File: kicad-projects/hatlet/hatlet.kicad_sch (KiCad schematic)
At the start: 14 parts, among them U1 RP2040

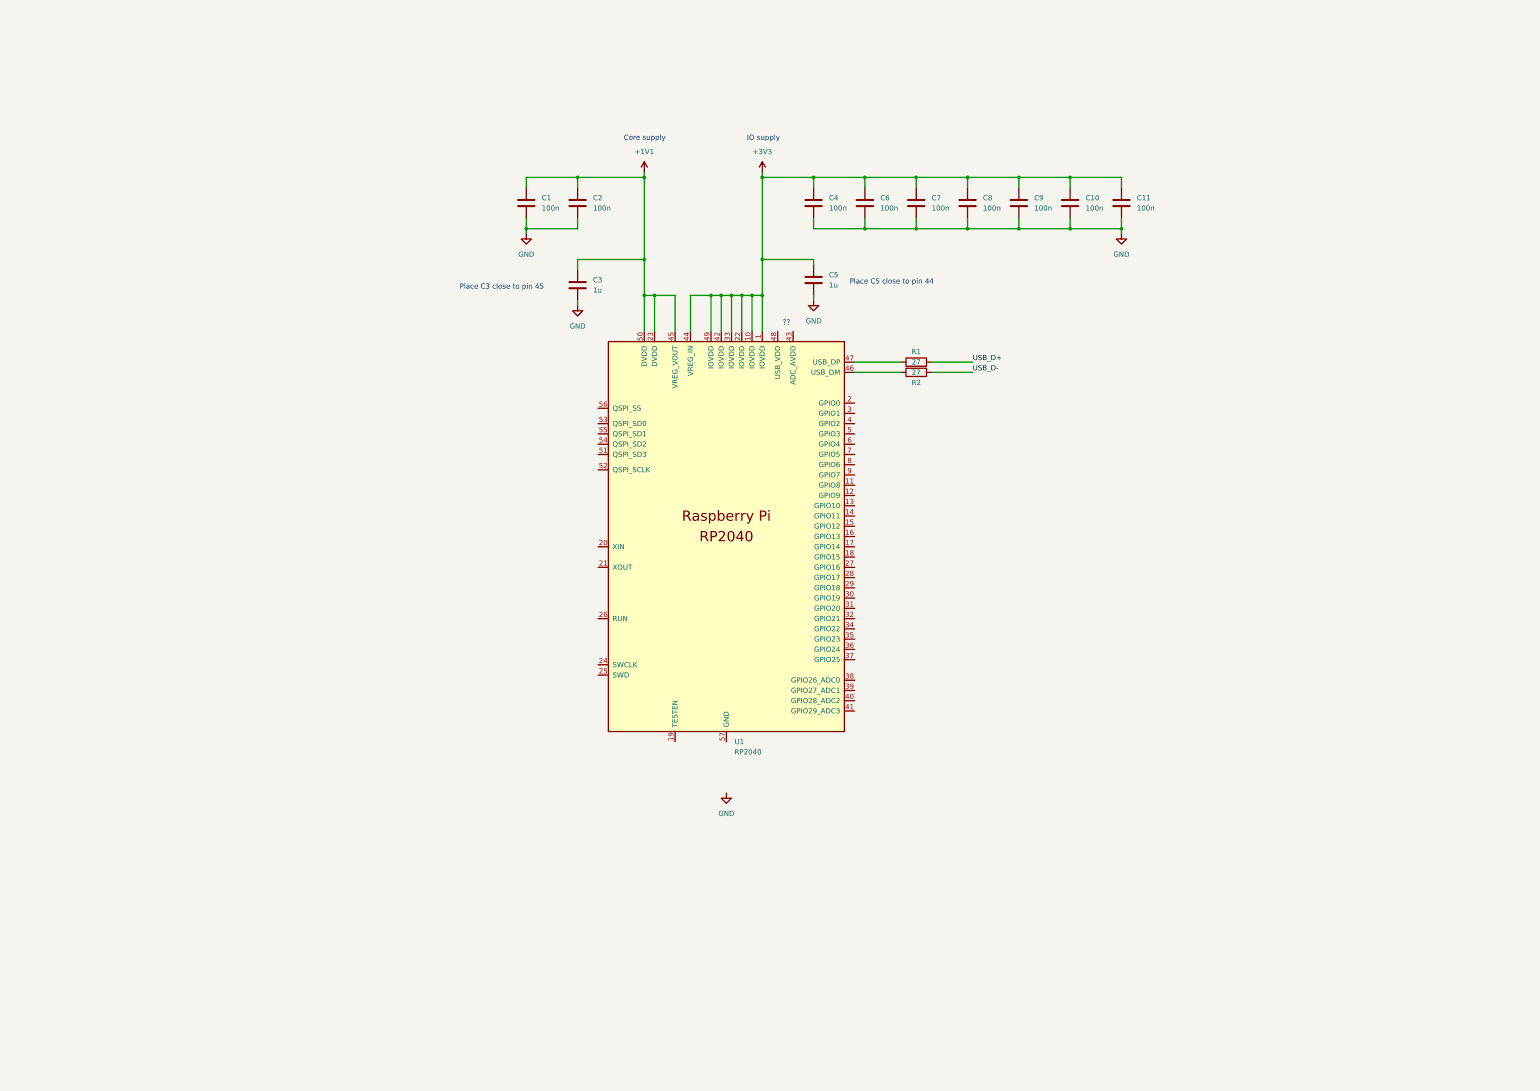
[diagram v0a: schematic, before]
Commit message: Update to KiCad 7
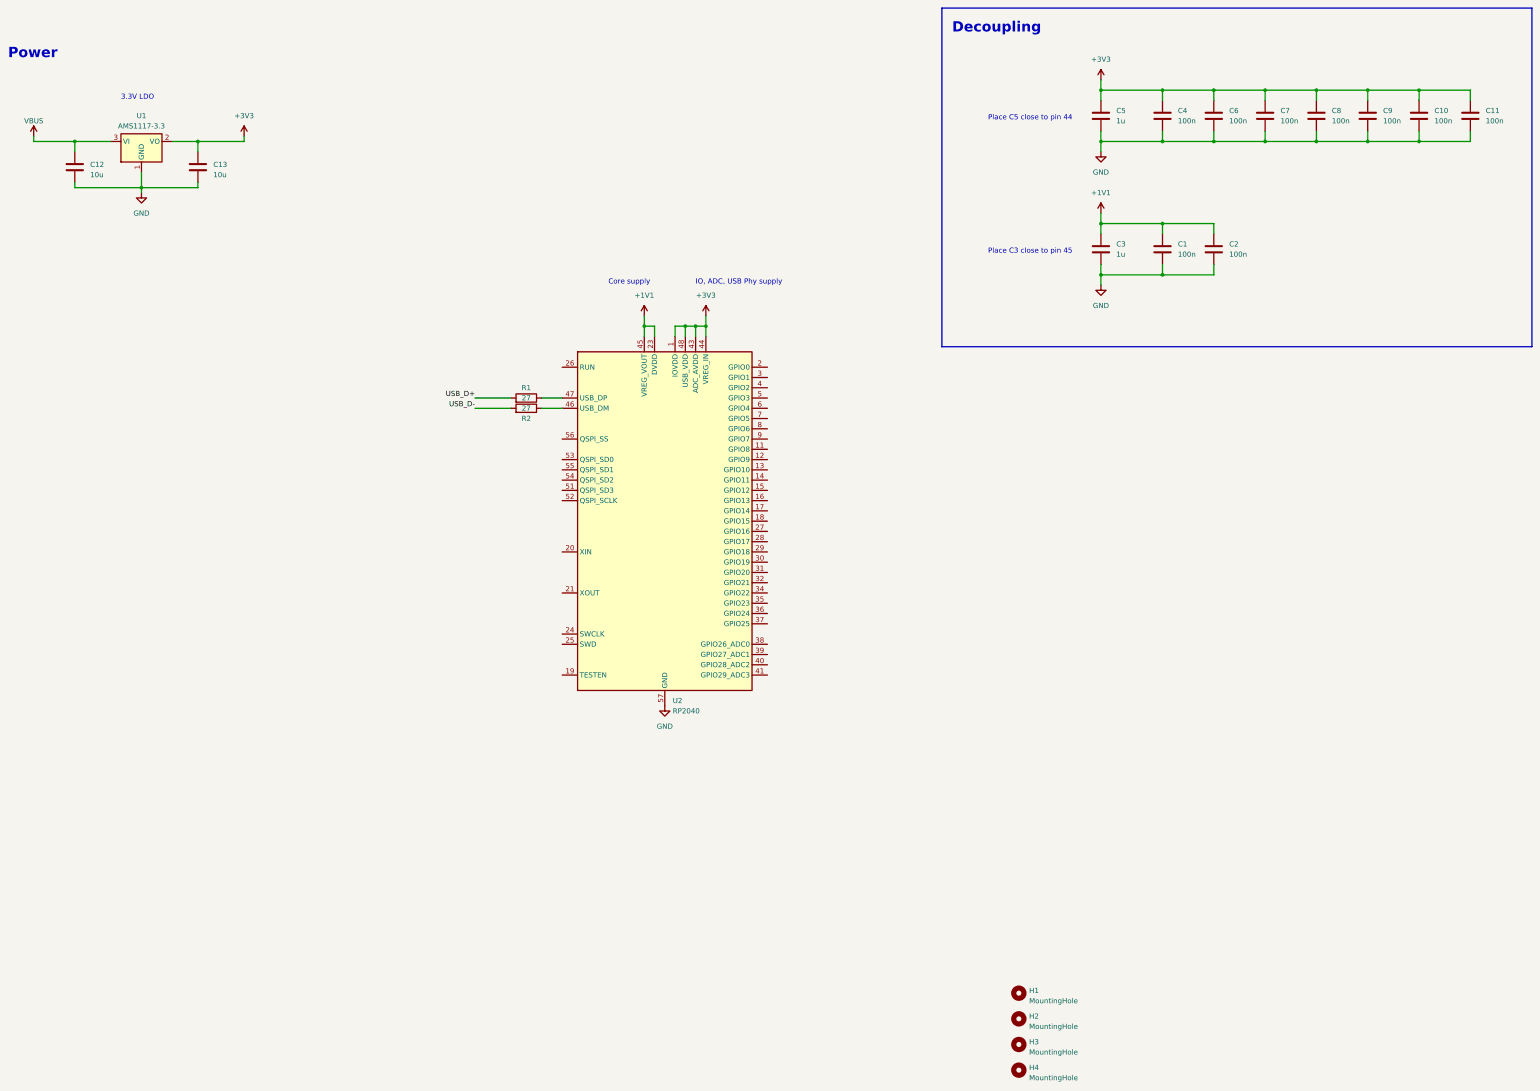
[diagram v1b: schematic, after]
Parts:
- removed U1: RP2040, racklet:RP2040-QFN-56, symbol racklet:RP2040
- added C12, C13: 10u, symbol Device:C
- added H1, H2, H3, H4: MountingHole, symbol Mechanical:MountingHole
- added U1: AMS1117-3.3, Package_TO_SOT_SMD:SOT-223-3_TabPin2, symbol Regulator_Linear:AMS1117-3.3
- added U2: RP2040, Package_DFN_QFN:QFN-56-1EP_7x7mm_P0.4mm_EP3.2x3.2mm, symbol MCU_RaspberryPi:RP2040
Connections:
- net +1V1: now also U2.23 (DVDD), U2.45 (VREG_VOUT), U2.50 (DVDD)
- net +3V3: now also C13.1, U1.2 (VO), U2.1 (IOVDD), U2.10 (IOVDD), U2.22 (IOVDD), U2.33 (IOVDD), U2.42 (IOVDD), U2.43 (ADC_AVDD), U2.44 (VREG_IN), U2.48 (USB_VDD), U2.49 (IOVDD)
- net GND: now also C12.2, C13.2, U1.1 (GND), U2.57 (GND)
- net at R2.1: now also U2.46 (USB_DM)
- net at R1.1: now also U2.47 (USB_DP)
- new net VBUS: C12.1, U1.3 (VI)
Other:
- note added: "3.3V LDO"
- note added: "Decoupling"
- note added: "IO, ADC, USB Phy supply"
- note added: "Power"
- note removed: "??"
- note removed: "IO supply"
- moved on the sheet: C1, C10, C11, C2, C3, C4, C5, C6, C7, C8, C9, R1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

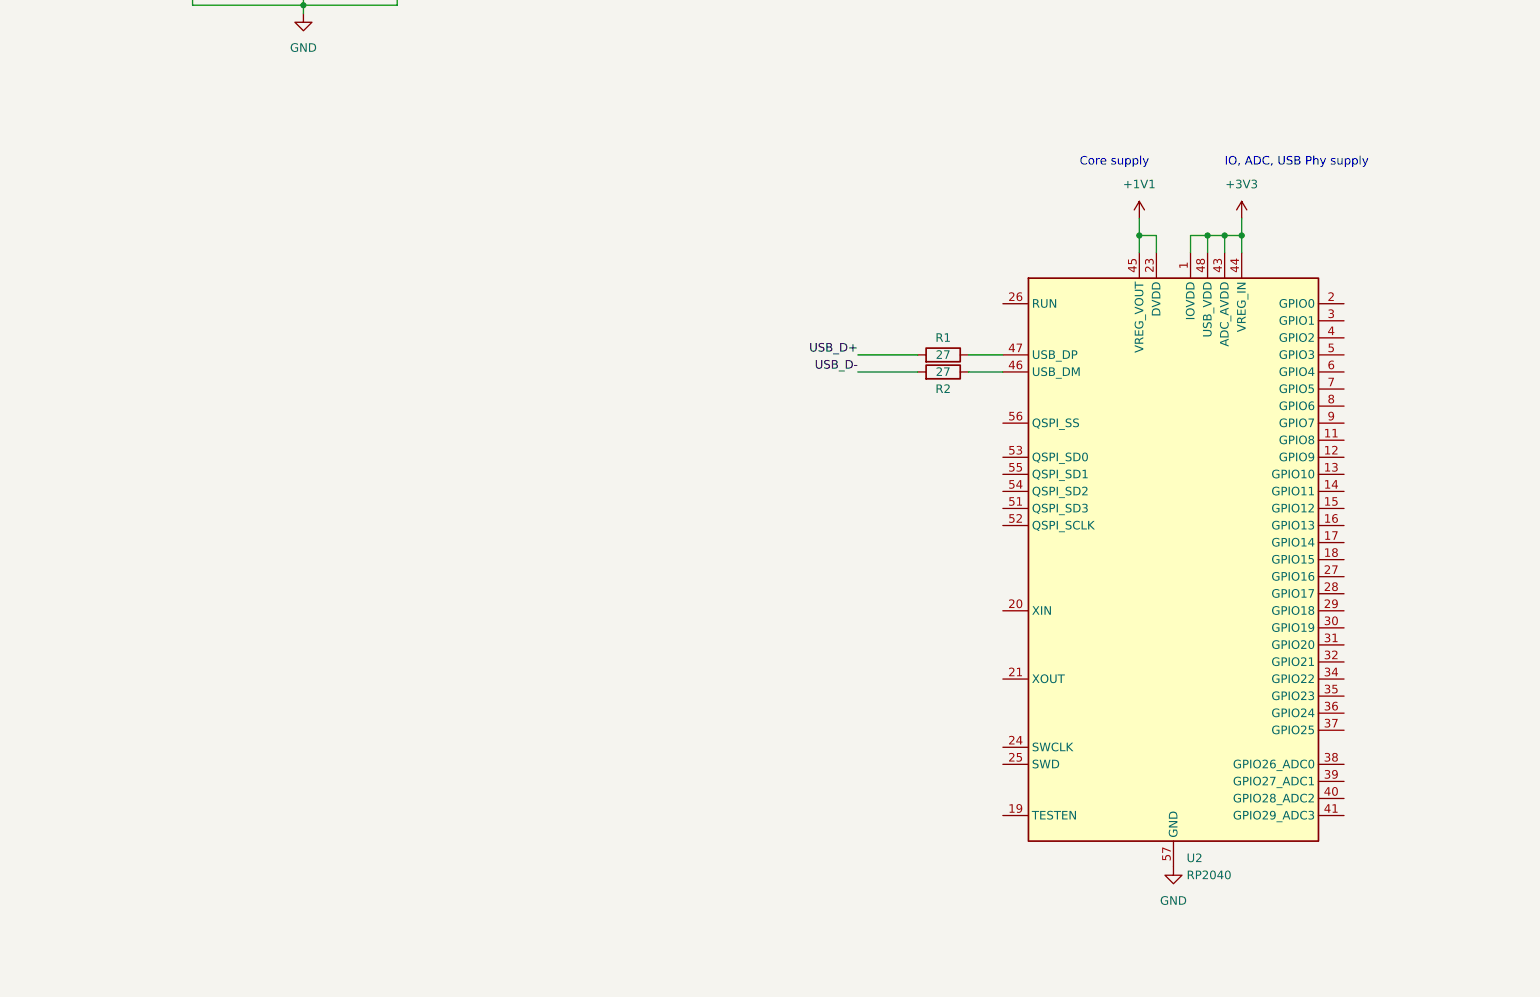
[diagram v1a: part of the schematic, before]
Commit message: Add USB "PMOD" connector
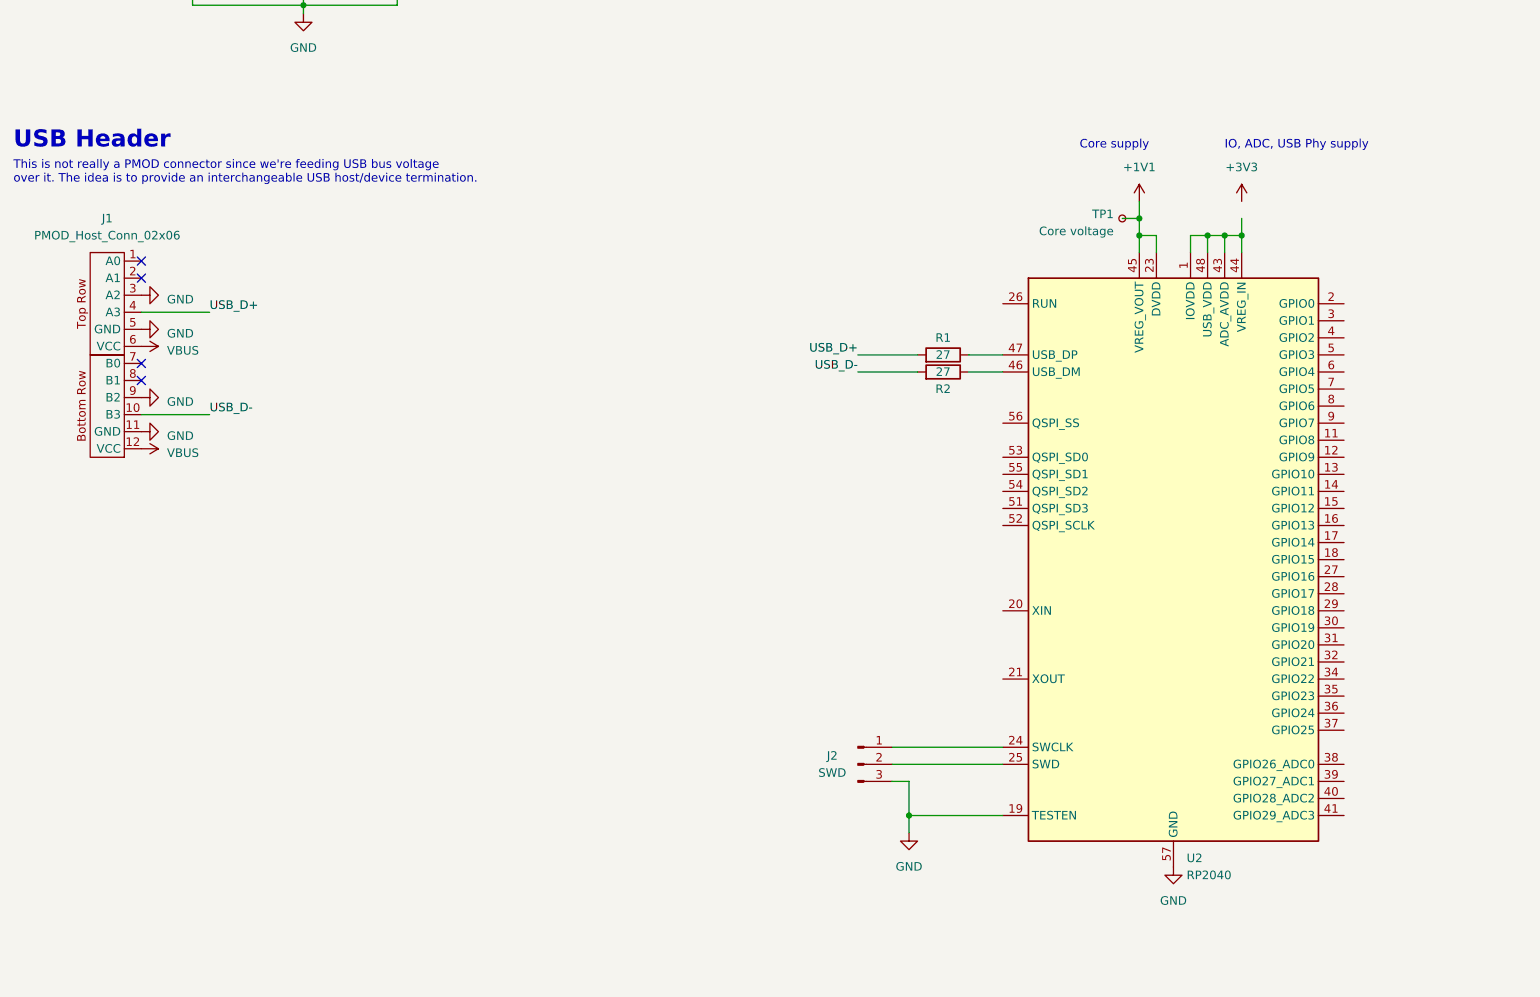
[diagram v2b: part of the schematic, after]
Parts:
- added J1: PMOD_Host_Conn_02x06, pmod:PMOD_PinSocket_2x06_P2.54mm_Horizontal, symbol pmod:PMOD_Host_Conn_02x06
- added J2: SWD, symbol Connector:Conn_01x03_Pin
- added TP1: Core voltage, symbol Connector:TestPoint_Small
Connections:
- net +1V1: now also TP1.1
- net +3V3: no longer U2.1 (IOVDD), U2.10 (IOVDD), U2.22 (IOVDD), U2.33 (IOVDD), U2.42 (IOVDD), U2.43 (ADC_AVDD), U2.44 (VREG_IN), U2.48 (USB_VDD), U2.49 (IOVDD)
- net GND: now also U2.19 (TESTEN), J1.11 (GND), J1.3 (A2), J1.5 (GND), J1.9 (B2), J2.3 (Pin_3)
- net USB_D+: now also J1.4 (A3)
- net USB_D-: now also J1.10 (B3)
- net VBUS: now also J1.12 (VCC), J1.6 (VCC)
- net at U2.24 (SWCLK): now also J2.1 (Pin_1)
- net at U2.25 (SWD): now also J2.2 (Pin_2)
- new net: U2.1 (IOVDD), U2.10 (IOVDD), U2.22 (IOVDD), U2.33 (IOVDD), U2.42 (IOVDD), U2.43 (ADC_AVDD), U2.44 (VREG_IN), U2.48 (USB_VDD), U2.49 (IOVDD)
- no-connect marks 0 -> 4
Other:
- note added: "This is not really a PMOD connector since we're feeding USB bus voltage over it. The idea is to provide an interchangeable USB host/device termination."
- note added: "USB Header"

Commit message: Add SPI flash, BOOTSEL button
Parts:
- removed H1, H2, H3, H4: MountingHole, symbol Mechanical:MountingHole
- added C14: 100N, symbol Device:C_Small
- added H1, H2, H3, H4: MH, MountingHole:MountingHole_3.2mm_M3_Pad_Via, symbol Mechanical:MountingHole_Pad
- added R3: 10k, symbol Device:R
- added R4: 1k, symbol Device:R
- added SW1: BOOTSEL, symbol Switch:SW_Push
- added U3: W25Q128JVS, Package_SO:SOIC-8_5.23x5.23mm_P1.27mm, symbol Memory_Flash:W25Q128JVS
- C1, C10, C11, C12, C13, C2, C3, C4, C5, C6, C7, C8, C9: footprint (none) -> Capacitor_SMD:C_0603_1608Metric
- J1: value PMOD_Host_Conn_02x06 -> USB Header
- J2: footprint (none) -> Connector_PinHeader_2.54mm:PinHeader_1x03_P2.54mm_Vertical
- R1, R2: footprint (none) -> Resistor_SMD:R_0603_1608Metric
- TP1: footprint (none) -> TestPoint:TestPoint_Pad_D1.0mm
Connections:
- net +3V3: now also U2.1 (IOVDD), U2.10 (IOVDD), U2.22 (IOVDD), U2.33 (IOVDD), U2.42 (IOVDD), U2.43 (ADC_AVDD), U2.44 (VREG_IN), U2.48 (USB_VDD), U2.49 (IOVDD), C14.1, R3.1, U3.8 (VCC)
- net GND: now also C14.2, H1.1, H2.1, H3.1, H4.1, R4.2, U3.4 (GND)
- net QSPI_SD3: now reaches U2.51 (QSPI_SD3)
- net QSPI_SD3: now also U3.7 (IO3)
- net QSPI_CLK: now reaches U2.52 (QSPI_SCLK)
- net QSPI_CLK: now also U3.6 (CLK)
- net QSPI_SD0: now reaches U2.53 (QSPI_SD0)
- net QSPI_SD0: now also U3.5 (DI(IO0))
- net QSPI_SD2: now reaches U2.54 (QSPI_SD2)
- net QSPI_SD2: now also U3.3 (IO2)
- net QSPI_SD1: now reaches U2.55 (QSPI_SD1)
- net QSPI_SD1: now also U3.2 (DO(IO1))
- net QSPI_CS: now reaches U2.56 (QSPI_SS)
- net QSPI_CS: now also R3.2, SW1.1, U3.1 (~{CS})
- new net: R4.1, SW1.2
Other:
- note added: "Boot Mode Selection"
- note added: "Mounting holes"
- note added: "Push BOOTSEL to enter USB DFU mode"
- moved on the sheet: C1, C10, C11, C2, C3, C4, C5, C6, C7, C8, C9

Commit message: Add crystal
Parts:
- added C15, C16: 27p, symbol Device:C_Small
- added R5: 1k, symbol Device:R_Small
- added Y1: Crystal_GND24, Crystal:Crystal_SMD_3225-4Pin_3.2x2.5mm, symbol Device:Crystal_GND24
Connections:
- net +3V3: now also U2.26 (RUN)
- net GND: now also C15.2, C16.2, Y1.2, Y1.4
- net I2C0_SDA: now reaches U2.2 (GPIO0)
- net XIN: now reaches U2.20 (XIN)
- net XIN: now also C15.1, Y1.1
- net XOUT: now reaches U2.21 (XOUT)
- net XOUT: now also R5.2
- net I2C0_SCL: now reaches U2.3 (GPIO1)
- net I2C1_SDA: now reaches U2.4 (GPIO2)
- net I2C1_SCL: now reaches U2.5 (GPIO3)
- net SPI0_MISO: now reaches U2.6 (GPIO4)
- net SPI0_CSn: now reaches U2.7 (GPIO5)
- net SPI0_SCK: now reaches U2.8 (GPIO6)
- net SPI0_MOSI: now reaches U2.9 (GPIO7)
- new net: C16.1, R5.1, Y1.3
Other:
- note added: "Crystal Oscillator"
- note added: "Differential 90 ohm board thickness: 1.0mm width: 0.8mm separation: 0.15mm"
- note added: "Global async reset tie to IOVDD to disable"
- note added: "Good to have connections: - SPI - I2C - UART"
- note added: "I2C 0 I2C 1"
- note added: "PMOD0"
- note added: "PMOD1"
- note added: "QSPI Flash"
- note added: "SPI 0"
- note added: "USB Host/Device and speed identification resistors are integrated to RP2040"
- note added: "YSX321SL: C_{L} = 20pF Assuming parasitic capacitance of around 5pF gives C_{1}=C_{2} = 30pF ~ 27pF"
- moved on the sheet: C14, J1, J2, R1, R2, TP1, U2, U3

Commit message: WIP: start fleshing out PMOD headers
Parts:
- added D1: LED0, LED_SMD:LED_0201_0603Metric, symbol Device:LED_Small
- added D2: LED1, LED_SMD:LED_0201_0603Metric, symbol Device:LED_Small
- added J3: PMOD0, pmod:PMOD_PinSocket_2x06_P2.54mm_Horizontal, symbol pmod:PMOD_Host_Conn_02x06
- added J4: PMOD2, pmod:PMOD_PinSocket_2x06_P2.54mm_Horizontal, symbol pmod:PMOD_Host_Conn_02x06
- added J5: PMOD1, pmod:PMOD_PinSocket_2x06_P2.54mm_Horizontal, symbol pmod:PMOD_Host_Conn_02x06
- added R6, R7: 1k, Resistor_SMD:R_0603_1608Metric, symbol Device:R_Small
- C1, C10, C11, C2, C3, C4, C5, C6, C7, C8, C9: symbol Device:C -> Device:C_Small
- C14: value 100N -> 100n; footprint (none) -> Capacitor_SMD:C_0201_0603Metric
- C15, C16: footprint (none) -> Capacitor_SMD:C_0201_0603Metric
- R3, R4, R5: footprint (none) -> Resistor_SMD:R_0603_1608Metric
- SW1: footprint (none) -> Button_Switch_SMD:SW_SPST_SKQG_WithStem
- Y1: value Crystal_GND24 -> Crystal 12MHz
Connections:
- net +3V3: now also J3.12 (VCC), J3.6 (VCC), J4.12 (VCC), J4.6 (VCC), J5.12 (VCC), J5.6 (VCC)
- net GND: now also J3.11 (GND), J3.5 (GND), J4.11 (GND), J4.5 (GND), J5.11 (GND), J5.5 (GND), R6.2, R7.2
- net I2C0_SCL: now also U2.7 (GPIO5), J3.4 (A3); no longer U2.3 (GPIO1)
- net I2C0_SDA: now also U2.6 (GPIO4), J3.3 (A2); no longer U2.2 (GPIO0)
- net I2C1_SCL: now also U2.12 (GPIO9), J3.10 (B3); no longer U2.5 (GPIO3)
- net I2C1_SDA: now also U2.11 (GPIO8), J3.9 (B2); no longer U2.4 (GPIO2)
- net SPI0_CSn: now also U2.32 (GPIO21), J4.1 (A0); no longer U2.7 (GPIO5)
- net SPI0_MISO: now also U2.31 (GPIO20), J4.3 (A2); no longer U2.6 (GPIO4)
- net SPI0_MOSI: now also U2.30 (GPIO19), J4.2 (A1); no longer U2.9 (GPIO7)
- net SPI0_SCK: now also U2.29 (GPIO18), J4.4 (A3); no longer U2.8 (GPIO6)
- net SPI1_SCK: now reaches U2.13 (GPIO10)
- net SPI1_SCK: now also J5.4 (A3)
- net SPI1_MOSI: now reaches U2.14 (GPIO11)
- net SPI1_MOSI: now also J5.2 (A1)
- net SPI1_MISO: now reaches U2.15 (GPIO12)
- net SPI1_MISO: now also J5.3 (A2)
- net SPI1_CSn: now reaches U2.16 (GPIO13)
- net SPI1_CSn: now also J5.1 (A0)
- net SPI1_INT: now reaches U2.17 (GPIO14)
- net SPI1_INT: now also J5.7 (B0)
- net SPI1_RESET: now reaches U2.18 (GPIO15)
- net SPI1_RESET: now also J5.8 (B1)
- net SPI0_INT: now reaches U2.34 (GPIO22)
- net SPI0_INT: now also J4.7 (B0)
- net SPI0_RESET: now reaches U2.35 (GPIO23)
- net SPI0_RESET: now also J4.8 (B1)
- new net: D2.1 (K), R7.1
- new net: D1.1 (K), R6.1
- new net I2C0_INT: J3.1 (A0), U2.4 (GPIO2)
- new net I2C0_RESET: J3.2 (A1), U2.5 (GPIO3)
- new net I2C1_INT: J3.7 (B0), U2.8 (GPIO6)
- new net I2C1_RESET: J3.8 (B1), U2.9 (GPIO7)
- new net LED0: D1.2 (A), U2.2 (GPIO0)
- new net LED1: D2.2 (A), U2.3 (GPIO1)
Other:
- note added: "-- I2C PMOD -- 1 ~{INT} 2 RESET 3 SCL 4 SDA"
- note added: "-- SPI PMOD -- 1 CS 2 MOSI 3 MISO 4 SCK 7 INT 8 RESET 9 N/S 10 N/S"
- note added: "-- top row -- 1 I2C0 ~{INT} (GPIO2) 2 I2C0 RESET (GPIO3) 3 I2C0 SCL (GPIO4) 4 I2C0 SDA (GPIO5) 5 GND 6 VCC -- bottom row -- 7 I2C1 ~{INT} (GPIO6) 8 I2C1 RESET (GPIO7) 9 I2C1 SCL (GPIO8) 10 I2C1 SDA (GPIO9) 11 GND 12 VCC"
- note added: "-- top row -- 1 SPI1 ~{CS} (GPIO13) 2 SPI1 MOSI (GPIO11) 3 SPI1 MISO (GPIO12) 4 SPI1 SCK (GPIO10) 5 GND 6 VCC -- bottom row -- 7 SPI0 INT (GPIO14) 8 SPI0 RESET (GPIO15) 9 N/S 10 N/S 11 GND 12 VCC"
- note added: "1"
- note added: "10"
- note added: "11"
- note added: "12"
- note added: "2"
- note added: "3"
- note added: "4"
- note added: "5"
- note added: "6"
- note added: "7"
- note added: "8"
- note added: "9"
- note added: "Blink blink :)"
- note added: "Good to have: - LEDs! - SPI PMOD - I2C PMOD - UART PMOD"
- note added: "Looking into PMOD pin socket"
- note added: "PMOD Socket Pinout"
- note added: "PMOD0 Pinout (Dual I2C)"
- note added: "PMOD1 Pinout (SPI)"
- note added: "PMOD2 Pinout (SPI)"
- note removed: "Good to have connections: - SPI - I2C - UART"
- note removed: "I2C 0 I2C 1"
- note removed: "PMOD0"
- note removed: "PMOD1"
- note removed: "SPI 0"
- moved on the sheet: C1, C10, C11, C12, C13, C14, C15, C16, C2, C3, C4, C5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
